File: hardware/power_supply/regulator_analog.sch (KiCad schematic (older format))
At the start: 81 parts

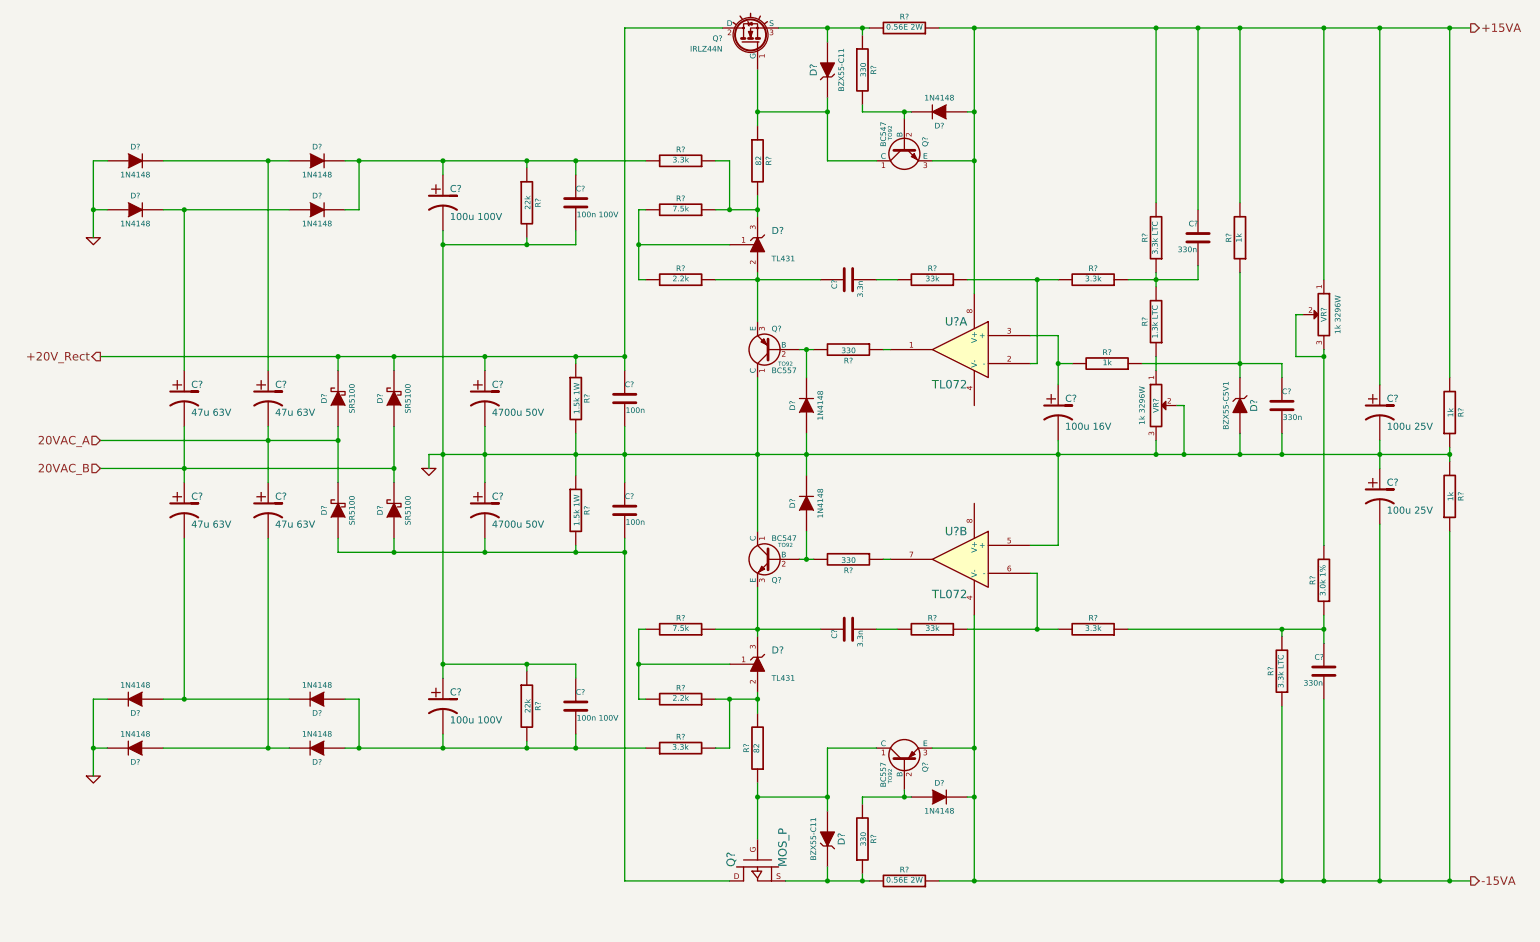
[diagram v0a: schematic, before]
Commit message: Update: almost finished power supply schematic (incl. +24V)
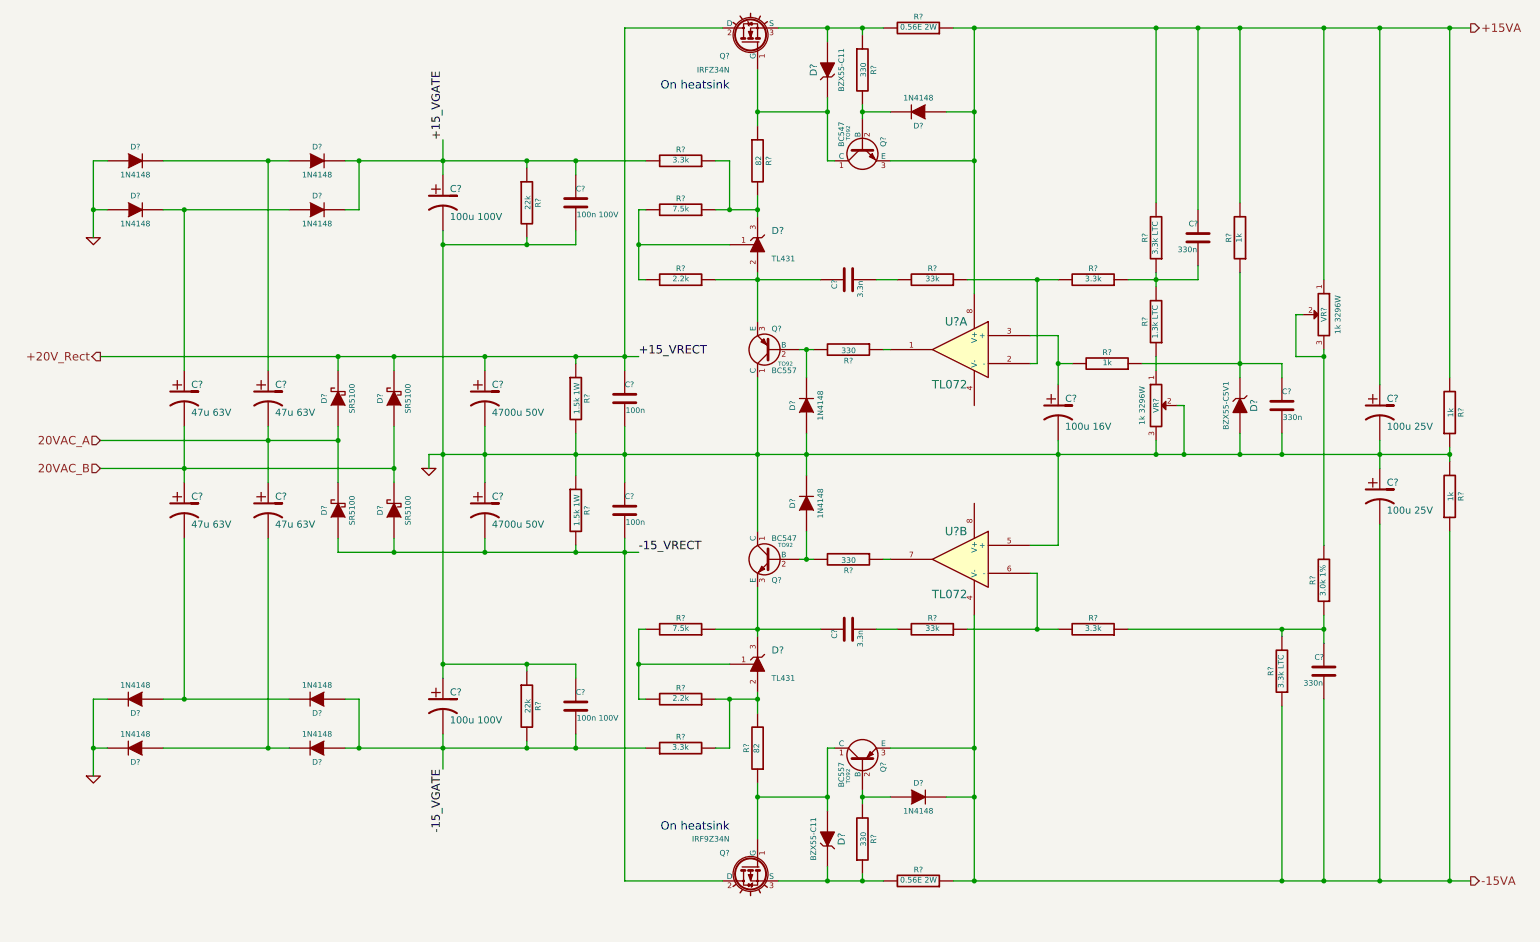
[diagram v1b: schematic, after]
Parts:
- removed Q?: MOS_P, symbol MOS_P
- removed Q?: IRLZ44N, symbol IRLZ44N
- added Q?: IRFZ34N, symbol MOS_N_IRF
- added Q?: IRF9Z34N, symbol MOS_P_IRF
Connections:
- net +20V_Rect: now also Q?.2 (D)
- net -15_VRECT: now reaches C?.2, C?.2, D?.1 (A), D?.1 (A), R?.2
- net -15_VRECT: now also Q?.2 (D)
- net +15_VGATE: now reaches C?.1, C?.1, D?.2 (K), D?.2 (K), R?.1, R?.2
- net -15_VGATE: now reaches C?.2, C?.2, D?.1 (A), D?.1 (A), R?.1, R?.2
- net at D?.1 (A), Q?.1 (C), R?.1: now also Q?.1 (G)
- net at D?.2 (K), R?.1, R?.2: now also Q?.3 (S)
- net at D?.2 (K), Q?.1 (C), R?.1: now also Q?.1 (G)
- net at D?.1 (A), R?.1, R?.2: now also Q?.3 (S)
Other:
- note added: "On heatsink"
- moved on the sheet: D?, Q?, R?

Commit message: Update: PCB, schematic fixes -Almost completed power supply PCB -Removed discharge resistors from +-15, +24V supplies: no place on PCB for them -Removed ceramic capacitors (stayed in parallel with electrolytic caps): no reason for them
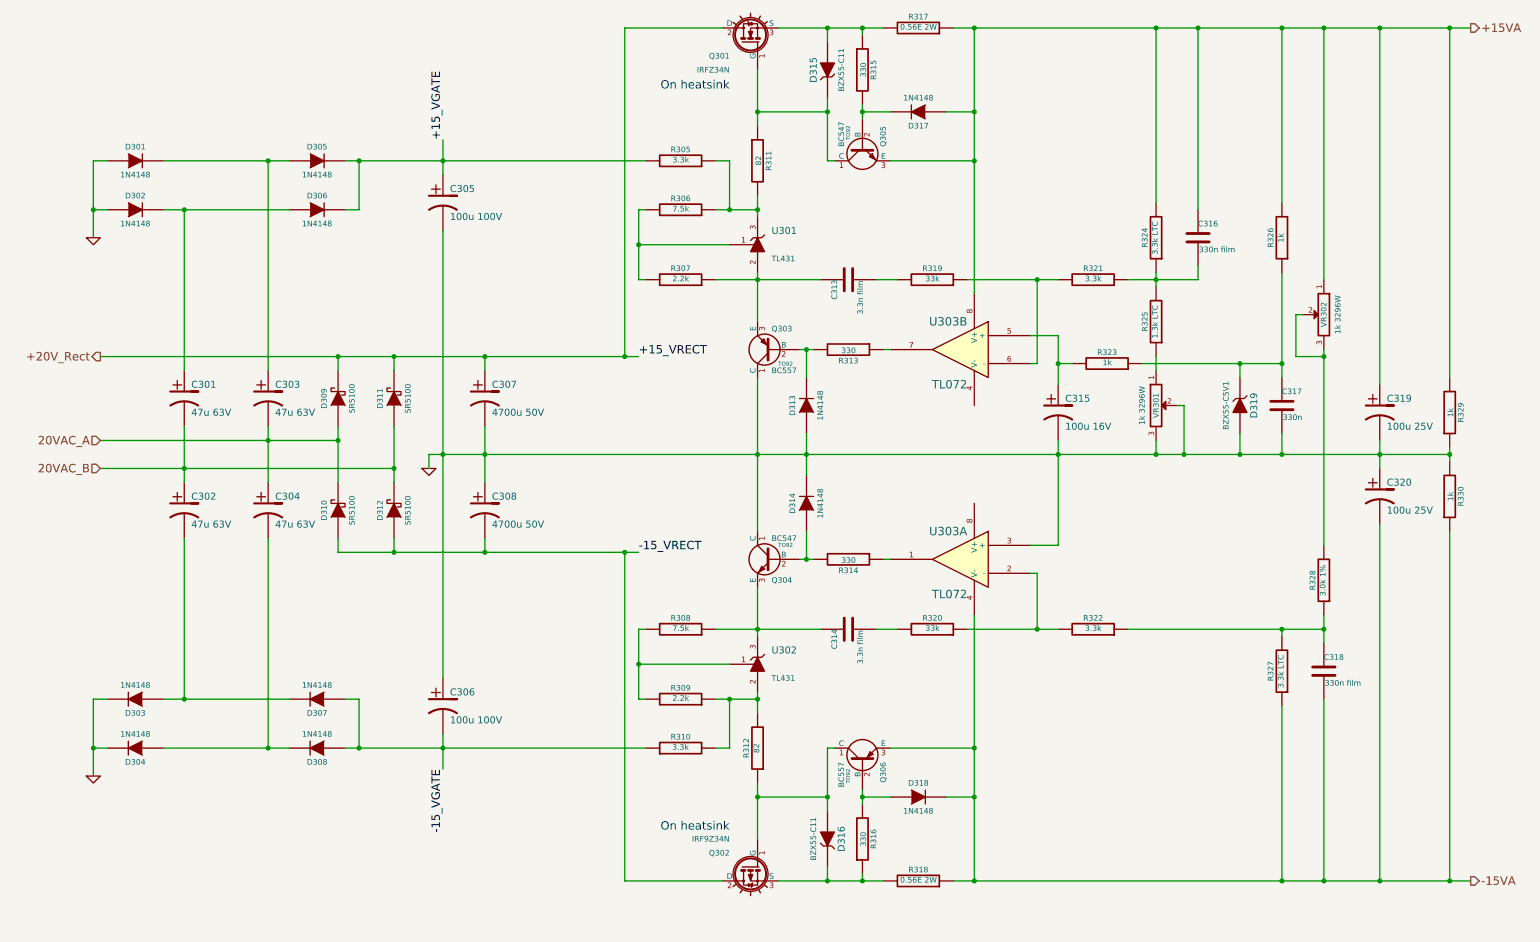
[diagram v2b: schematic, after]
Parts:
- removed C? (x2): 100n, symbol C
- removed C? (x2): 100n 100V, symbol C
- removed D? (x2): TL431, TO92, symbol TL431
- removed R? (x2): 1.5k 1W, symbol R
- removed R? (x2): 22k, symbol R
- added U301, U302: TL431, TO92, symbol TL431
- C313, C314: renamed from C?; value 3.3n -> 3.3n film
- C316, C318: renamed from C?; value 330n -> 330n film
- gave numbers to parts that had none: 66
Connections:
- net GND: now also U303.3 (+); no longer U303.5 (+)
- net at R313.1: now also U303.7; no longer U303.1
- net at R319.1, R321.2: now also U303.6 (-); no longer U303.2 (-)
- net at C315.1, R323.2: now also U303.5 (+); no longer U303.3 (+)
- net at R320.1, R322.2: now also U303.2 (-); no longer U303.6 (-)
- net at R314.1: now also U303.1; no longer U303.7
- net at C314.1, Q304.3 (E), R308.1: now also U302.3 (K)
- net at C313.1, Q303.3 (E), R307.1: now also U301.2 (A)
- net at R306.2, R307.2: now also U301.1 (Ref)
- net at R305.1, R306.1, R311.2: now also U301.3 (K)
- net at R308.2, R309.2: now also U302.1 (Ref)
- net at R309.1, R310.2, R312.2: now also U302.2 (A)
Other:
- moved on the sheet: R326

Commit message: Update: fix schematic overlapping with page frame, add schematic in PDF
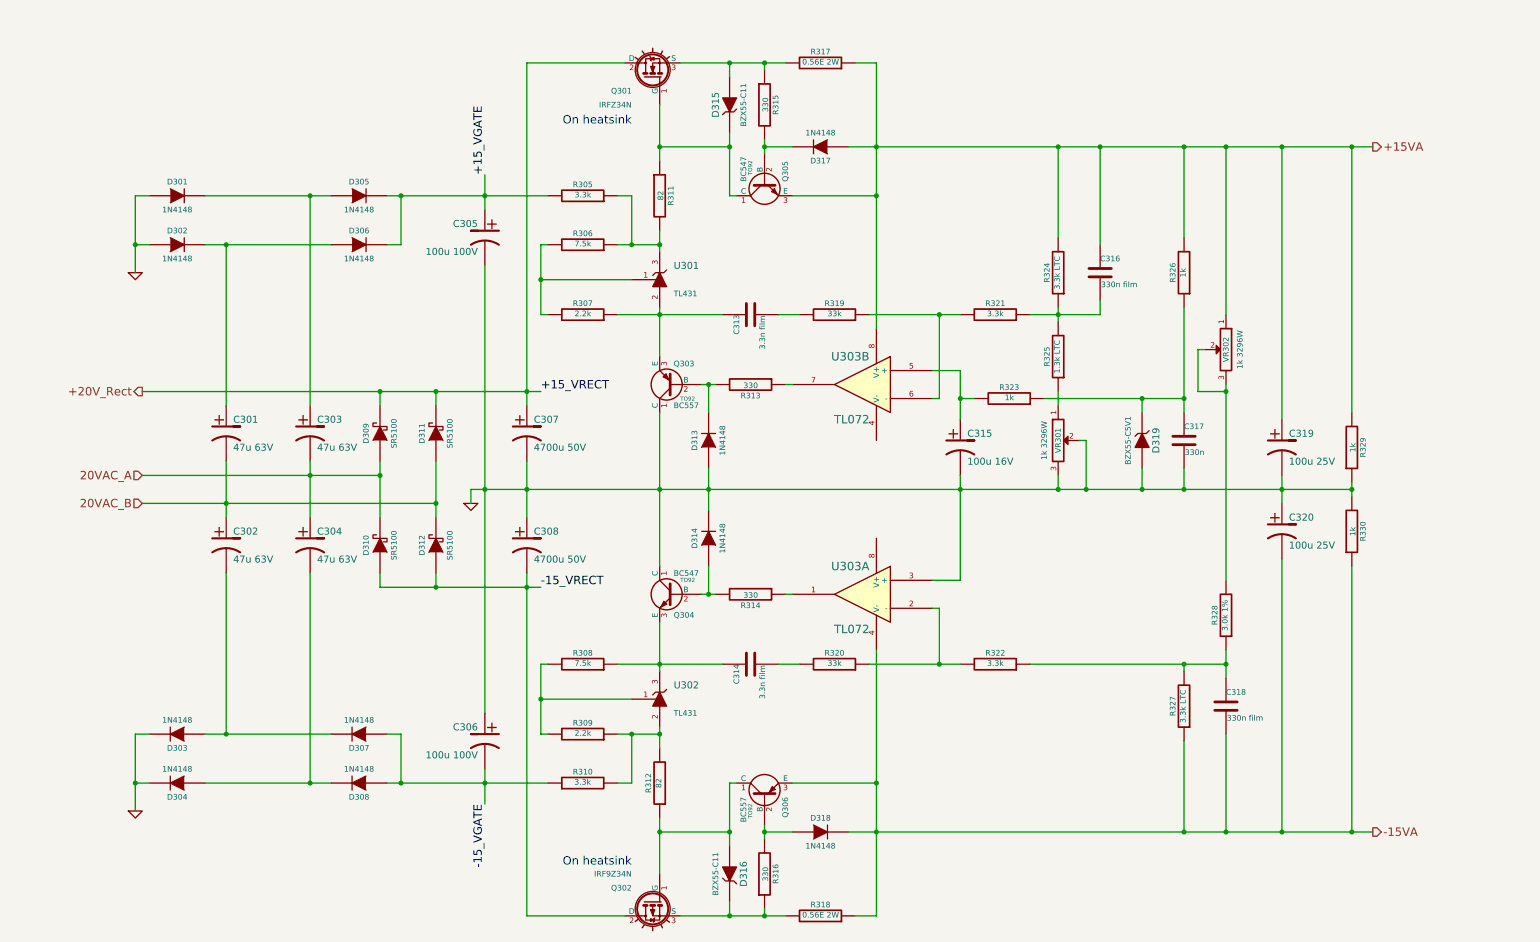
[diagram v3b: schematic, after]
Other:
- moved on the sheet: C301, C302, C303, C304, C305, C306, C307, C308, C313, C314, C315, C316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
